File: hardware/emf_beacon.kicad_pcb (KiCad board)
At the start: 2 copper layers, 100 x 100 mm, 133 parts, among them J1 USB_C_Receptacle_USB2.0_16P, J10 Conn_01x02, J11 Conn_01x02, J12 Conn_01x02, J13 Conn_01x02, J14 Conn_01x02, J2 B6B-PH-SM4-TB, J3 B6B-PH-SM4-TB, J4 Conn_01x02, J5 Conn_01x02, J6 Conn_01x02, J7 Conn_01x02, J8 Conn_01x02, J9 Conn_01x02, Q1 AO3400A, Q10 AO3400A, Q12 DMP3013SFV, Q2 AO3400A, Q3 AO3400A, Q4 AO3400A, Q5 AO3400A, Q6 AO3400A, Q7 AO3400A, Q8 AO3400A, Q9 AO3400A, SW1 SW_DIP_x10, SW2 TS-1088-AR02016, U1 ESP32-C3-WROOM-02, U2 MCP23017T-E/SS, U4 PCA9685PW,118, U5 TPS565208, U6 CA-IS3092W, U7 TPS82140SILR

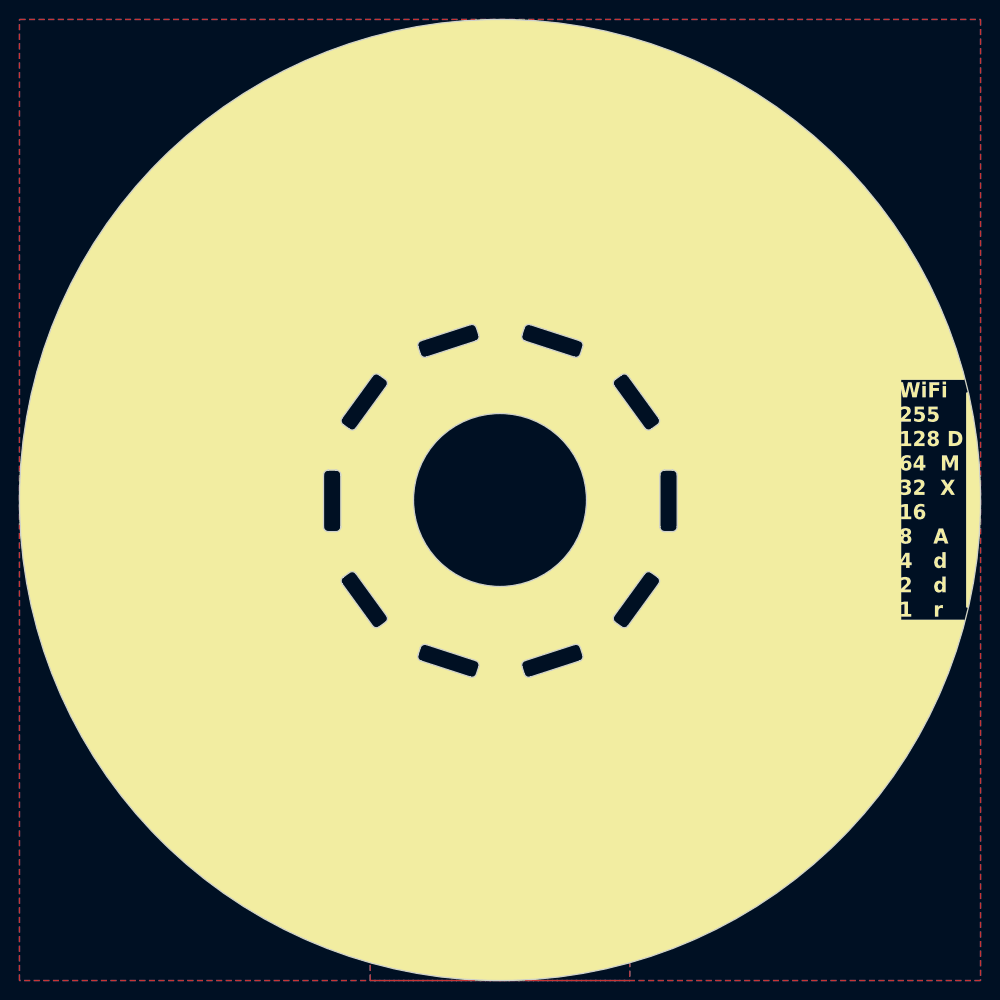
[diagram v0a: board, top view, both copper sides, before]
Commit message: finished USB routing
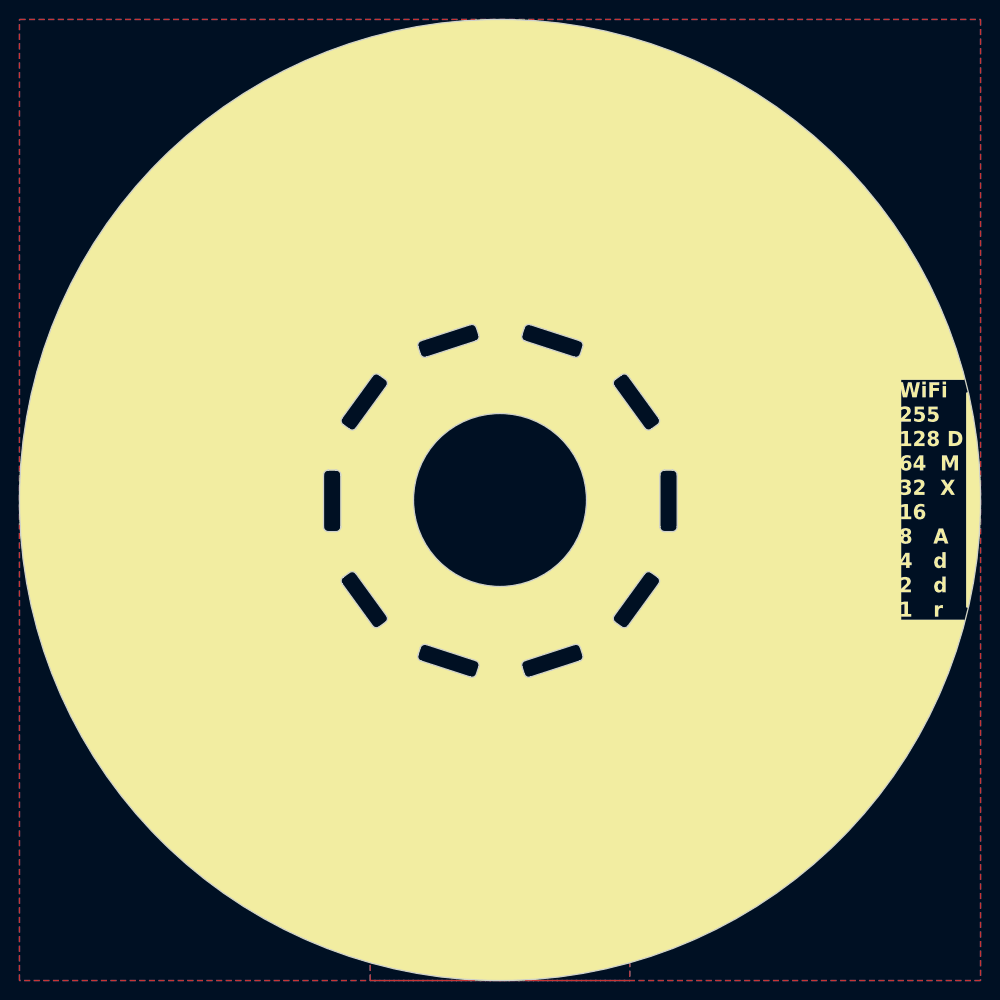
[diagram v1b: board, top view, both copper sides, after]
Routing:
- net /CTRL/USB-: track 19.7 -> 18.7 mm

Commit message: finished NTC routing
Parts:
- moved R3 2.02 mm to (134.8, 56.5), turned to -90 degrees
- moved C3 1.03 mm to (133.2, 56.5), turned to 90 degrees
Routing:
- net /CTRL/TEMP_MON: track 31.4 -> 60.6 mm, vias 1 -> 2
- net +3V3: track 236.9 -> 243.6 mm, vias 11 -> 12
- net GND: vias 117 -> 120
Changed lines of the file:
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@@
 	(footprint "Capacitor_SMD:C_0603_1608Metric"
 		(layer "B.Cu")
-		(at 134.25 56.25 -90)
+		(at 133.25 56.5 90)
 		(descr "Capacitor SMD 0603 (1608 Metric), square (rectangular) end terminal, IPC-7351 nominal, (Body size source: IPC-SM-782 page 76, https://www.pcb-3d.com/wordpress/wp-content/uploads/ipc-sm-782a_amendment_1_and_2.pdf), generated with kicad-footprint-generator")
 		(tags "capacitor")
 		(property "Reference" "C3"
-			(at 0 1.43 90)
+			(at 2.5 0 90)
 			(layer "B.SilkS")
 			(effects
@@
 		)
 		(property "MFR" ""
-			(at 0 0 270)
+			(at 0 0 90)
 			(unlocked yes)
 			(layer "B.Fab")
@@
 		)
 		(property "MPN" ""
-			(at 0 0 270)
+			(at 0 0 90)
 			(unlocked yes)
 			(layer "B.Fab")
@@
 		)
 		(property "LCSC" "C15849"
-			(at 0 0 270)
+			(at 0 0 90)
 			(unlocked yes)
 			(layer "B.Fab")
@@
 		(attr smd)
 		(fp_line
-			(start -0.14058 0.51)
-			(end 0.14058 0.51)
+			(start -0.14058 -0.51)
+			(end 0.14058 -0.51)
 			(stroke
 				(width 0.12)
@@
 		)
 		(fp_line
-			(start -0.14058 -0.51)
-			(end 0.14058 -0.51)
+			(start -0.14058 0.51)
+			(end 0.14058 0.51)
 			(stroke
 				(width 0.12)
@@
 		)
 		(pad "1" smd roundrect
-			(at -0.775 0 270)
+			(at -0.775 0 90)
 			(size 0.9 0.95)
 			(layers "B.Cu" "B.Mask" "B.Paste")
@@
 		)
 		(pad "2" smd roundrect
-			(at 0.775 0 270)
+			(at 0.775 0 90)
 			(size 0.9 0.95)
 			(layers "B.Cu" "B.Mask" "B.Paste")
@@
 	(footprint "Resistor_SMD:R_0603_1608Metric"
 		(layer "B.Cu")
-		(at 132.75 56.25 90)
+		(at 134.75 56.5 -90)
 		(descr "Resistor SMD 0603 (1608 Metric), square (rectangular) end terminal, IPC-7351 nominal, (Body size source: IPC-SM-782 page 72, https://www.pcb-3d.com/wordpress/wp-content/uploads/ipc-sm-782a_amendment_1_and_2.pdf), generated with kicad-footprint-generator")
 		(tags "resistor")
 		(property "Reference" "R3"
-			(at 0 1.43 90)
+			(at -2.5 0 90)
 			(layer "B.SilkS")
 			(effects
@@
 		)
 		(property "MFR" ""
-			(at 0 0 90)
+			(at 0 0 270)
 			(unlocked yes)
 			(layer "B.Fab")
@@
 		)
 		(property "MPN" ""
-			(at 0 0 90)
+			(at 0 0 270)
 			(unlocked yes)
 			(layer "B.Fab")
@@
 		)
 		(property "LCSC" "C25804"
-			(at 0 0 90)
+			(at 0 0 270)
 			(unlocked yes)
 			(layer "B.Fab")
@@
 		(attr smd)
 		(fp_line
-			(start -0.237258 -0.5225)
-			(end 0.237258 -0.5225)
+			(start -0.237258 0.5225)
+			(end 0.237258 0.5225)
 			(stroke
 				(width 0.12)
@@
 		)
 		(fp_line
-			(start -0.237258 0.5225)
-			(end 0.237258 0.5225)
+			(start -0.237258 -0.5225)
+			(end 0.237258 -0.5225)
 			(stroke
 				(width 0.12)
@@
 		)
 		(pad "1" smd roundrect
-			(at -0.825 0 90)
+			(at -0.825 0 270)
 			(size 0.8 0.95)
 			(layers "B.Cu" "B.Mask" "B.Paste")
@@
 		)
 		(pad "2" smd roundrect
-			(at 0.825 0 90)
+			(at 0.825 0 270)
 			(size 0.8 0.95)
 			(layers "B.Cu" "B.Mask" "B.Paste")
@@
 	)
 	(segment
-		(start 143.75 57.75)
-		(end 138.25 57.75)
-		(width 0.5)
-		(layer "F.Cu")
-		(net 1)
-	)
-	(segment
 		(start 177 122.25)
 		(end 180.75 122.25)
@@
 	)
 	(segment
+		(start 143.75 57.75)
+		(end 145.75 59.75)
+		(width 0.25)
+		(layer "F.Cu")
+		(net 1)
+	)
+	(segment
 		(start 164 61.5)
 		(end 164.75 62.25)
@@
 	)
 	(segment
-		(start 145.75 59.75)
-		(end 143.75 57.75)
-		(width 0.5)
+		(start 134.75 54.75)
+		(end 134.75 56.5)
+		(width 0.25)
 		(layer "F.Cu")
 		(net 1)
@@
 		(net 1)
 	)
+	(segment
+		(start 136 57.75)
+		(end 143.75 57.75)
+		(width 0.25)
+		(layer "F.Cu")
+		(net 1)
+	)
+	(segment
+		(start 134.75 56.5)
+		(end 136 57.75)
+		(width 0.25)
+		(layer "F.Cu")
+		(net 1)
+	)
 	(via
 		(at 123.75 78.75)
@@
 	)
 	(via
+		(at 134.75 54.75)
+		(size 0.6)
+		(drill 0.3)
+		(layers "F.Cu" "B.Cu")
+		(net 1)
+	)
+	(via
 		(at 165 56.5)
 		(size 0.6)
@@
 	)
 	(segment
+		(start 134.75 54.75)
+		(end 134.75 55.675)
+		(width 0.25)
+		(layer "B.Cu")
+		(net 1)
+	)
+	(segment
 		(start 187.975 76.75)
 		(end 187 76.75)
@@
 	)
 	(via
+		(at 124 60)
+		(size 0.6)
+		(drill 0.3)
+		(layers "F.Cu" "B.Cu")
+		(free yes)
+		(net 2)
+	)
+	(via
 		(at 146.25 125.25)
 		(size 0.6)
@@
 	)
 	(via
+		(at 133.25 54.75)
+		(size 0.6)
+		(drill 0.3)
+		(layers "F.Cu" "B.Cu")
+		(free yes)
+		(net 2)
+	)
+	(via
 		(at 111.25 109)
 		(size 0.6)
@@
 	)
 	(via
+		(at 144.25 59.5)
+		(size 0.6)
+		(drill 0.3)
+		(layers "F.Cu" "B.Cu")
+		(free yes)
+		(net 2)
+	)
+	(via
 		(at 161 59.75)
 		(size 0.6)
@@
 	)
 	(segment
-		(start 120.75 75.75)
-		(end 122 74.5)
+		(start 115.25 75.75)
+		(end 121.5 75.75)
 		(width 0.25)
 		(layer "F.Cu")
@@
 	)
 	(segment
-		(start 112.25 78.75)
-		(end 115.25 75.75)
+		(start 123.25 74)
+		(end 123.25 71.25)
 		(width 0.25)
 		(layer "F.Cu")
@@
 	)
 	(segment
-		(start 115.25 75.75)
-		(end 120.75 75.75)
+		(start 121.5 75.75)
+		(end 123.25 74)
+		(width 0.25)
+		(layer "F.Cu")
+		(net 84)
+	)
+	(segment
+		(start 112.25 78.75)
+		(end 115.25 75.75)
 		(width 0.25)
 		(layer "F.Cu")
@@
 	)
 	(via
+		(at 123.25 71.25)
+		(size 0.6)
+		(drill 0.3)
+		(layers "F.Cu" "B.Cu")
+		(net 84)
+	)
+	(via
 		(at 112.25 84.25)
 		(size 0.6)
@@
 	)
 	(segment
-		(start 141.25 57)
-		(end 137.5 57)
+		(start 133.3 57.325)
+		(end 134.75 57.325)
+		(width 0.25)
+		(layer "B.Cu")
+		(net 84)
+	)
+	(segment
+		(start 123.25 71.25)
+		(end 123.25 66.25)
+		(width 0.25)
+		(layer "B.Cu")
+		(net 84)
+	)
+	(segment
+		(start 133.25 57.275)
+		(end 133.3 57.325)
+		(width 0.25)
+		(layer "B.Cu")
+		(net 84)
+	)
+	(segment
+		(start 136.175 57.325)
+		(end 134.75 57.325)
+		(width 0.25)
+		(layer "B.Cu")
+		(net 84)
+	)
+	(segment
+		(start 123.25 66.25)
+		(end 122.75 65.75)
+		(width 0.25)
+		(layer "B.Cu")
+		(net 84)
+	)
+	(segment
+		(start 122.75 62.75)
+		(end 132.25 57.275)
 		(width 0.25)
 		(layer "B.Cu")
@@
 		(width 0.25)
 		(layer "B.Cu")
+		(net 84)
+	)
+	(segment
+		(start 122.75 65.75)
+		(end 122.75 62.75)
+		(width 0.25)
+		(layer "B.Cu")
+		(net 84)
+	)
+	(segment
+		(start 136.5 57)
+		(end 136.175 57.325)
+		(width 0.25)
+		(layer "B.Cu")
+		(net 84)
+	)
+	(segment
+		(start 141.25 57)
+		(end 136.5 57)
+		(width 0.25)
+		(layer "B.Cu")
+		(net 84)
+	)
+	(segment
+		(start 132.25 57.275)
+		(end 133.25 57.275)
+		(width 0.25)
+		(layer "B.Cu")

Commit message: ran DRC & DFM checks, looks good
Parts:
- moved D6 1.00 mm to (167.5, 64.5)
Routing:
- net Net-(D6-A): track 4.98 -> 5.98 mm
- net GND: vias 120 -> 122
- net +3V3: vias 12 -> 11
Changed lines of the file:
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@@
 			(unlocked yes)
 			(layer "B.SilkS")
+			(hide yes)
 			(effects
 				(font
@@
 			(unlocked yes)
 			(layer "B.SilkS")
+			(hide yes)
 			(effects
 				(font
@@
 		(tags "resistor")
 		(property "Reference" "TH1"
-			(at 0 1.43 90)
+			(at 0 -1.5 90)
 			(layer "B.SilkS")
 			(effects
@@
 	(footprint "Diode_SMD:D_SOD-323"
 		(layer "B.Cu")
-		(at 166.5 64.5 -90)
+		(at 167.5 64.5 -90)
 		(descr "SOD-323")
 		(tags "SOD-323")
@@
 		)
 		(fp_text user "${REFERENCE}"
-			(at 0 1.85 90)
+			(at 0 -1.75 90)
 			(layer "B.Fab")
 			(effects
@@
 			(unlocked yes)
 			(layer "B.SilkS")
+			(hide yes)
 			(effects
 				(font
@@
 			(unlocked yes)
 			(layer "B.SilkS")
+			(hide yes)
 			(effects
 				(font
@@
 		)
 		(fp_text user "${REFERENCE}"
-			(at 0 -2.5 180)
+			(at -1.25 -1.25 180)
 			(unlocked yes)
 			(layer "B.Fab")
@@
 			(unlocked yes)
 			(layer "B.SilkS")
+			(hide yes)
 			(effects
 				(font
@@
 			(unlocked yes)
 			(layer "B.SilkS")
+			(hide yes)
 			(effects
 				(font
@@
 			(unlocked yes)
 			(layer "B.SilkS")
+			(hide yes)
 			(effects
 				(font
@@
 			(unlocked yes)
 			(layer "B.SilkS")
+			(hide yes)
 			(effects
 				(font
@@
 			(unlocked yes)
 			(layer "B.SilkS")
+			(hide yes)
 			(effects
 				(font
@@
 			(unlocked yes)
 			(layer "B.SilkS")
+			(hide yes)
 			(effects
 				(font
@@
 	)
 	(via
-		(at 174.5 131.75)
-		(size 0.6)
-		(drill 0.3)
-		(layers "F.Cu" "B.Cu")
-		(net 1)
-	)
-	(via
 		(at 172.25 141)
 		(size 0.6)
@@
 	)
 	(via
+		(at 168.75 65.75)
+		(size 0.6)
+		(drill 0.3)
+		(layers "F.Cu" "B.Cu")
+		(free yes)
+		(net 2)
+	)
+	(via
 		(at 131.25 136)
 		(size 0.6)
@@
 	)
 	(via
+		(at 168.25 62.5)
+		(size 0.6)
+		(drill 0.3)
+		(layers "F.Cu" "B.Cu")
+		(free yes)
+		(net 2)
+	)
+	(via
 		(at 119 99.5)
 		(size 0.6)
@@
 	)
 	(segment
+		(start 166.5 61.5)
+		(end 167.5 62.5)
+		(width 0.25)
+		(layer "B.Cu")
+		(net 45)
+	)
+	(segment
 		(start 166.5 56.825)
 		(end 167.225 56.825)
@@
 	)
 	(segment
-		(start 167.725 57.325)
-		(end 167.725 59.5)
+		(start 167.5 62.5)
+		(end 167.5 63.45)
 		(width 0.25)
 		(layer "B.Cu")
@@
 	)
 	(segment
-		(start 165 59.075)
-		(end 165 60)
+		(start 167.725 57.325)
+		(end 167.725 59.5)
 		(width 0.25)
 		(layer "B.Cu")
@@
 	)
 	(segment
-		(start 166.5 61.5)
+		(start 165 59.075)
 		(end 165 60)
 		(width 0.25)
@@
 	)
 	(segment
-		(start 166.5 63.45)
-		(end 166.5 61.5)
+		(start 166.5 61.5)
+		(end 165 60)
 		(width 0.25)
 		(layer "B.Cu")
@@
 		(start 123.264898 119.689162)
 		(end 124.930635 121.3549)
-		(width 0.5)
+		(width 0.4)
 		(layer "B.Cu")
 		(net 59)
@@
 		(start 124.921663 121.085697)
 		(end 125.060751 121.224785)
-		(width 0.5)
+		(width 0.4)
 		(layer "B.Cu")
 		(net 59)
@@
 		(start 123.62868 122.37868)
 		(end 124.921663 121.085697)
-		(width 0.5)
+		(width 0.4)
 		(layer "B.Cu")
 		(net 59)
@@
 		(start 124.930635 121.3549)
 		(end 125.060751 121.224785)
-		(width 0.5)
+		(width 0.4)
 		(layer "B.Cu")
 		(net 59)
@@
 	)
 	(segment
-		(start 166.5 65.55)
-		(end 166.5 66.5)
+		(start 164.7 67.25)
+		(end 164.75 67.3)
 		(width 0.25)
 		(layer "B.Cu")
@@
 	)
 	(segment
-		(start 164.7 67.25)
-		(end 164.75 67.3)
+		(start 162.825 67.25)
+		(end 164.7 67.25)
 		(width 0.25)
 		(layer "B.Cu")
@@
 	)
 	(segment
-		(start 162.825 67.25)
-		(end 164.7 67.25)
+		(start 164.75 67.3)
+		(end 166.7 67.3)
 		(width 0.25)
 		(layer "B.Cu")
@@
 	)
 	(segment
-		(start 165.7 67.3)
-		(end 164.75 67.3)
+		(start 167.5 66.5)
+		(end 167.5 65.55)
 		(width 0.25)
 		(layer "B.Cu")
@@
 	)
 	(segment
-		(start 166.5 66.5)
-		(end 165.7 67.3)
+		(start 166.7 67.3)
+		(end 167.5 66.5)
 		(width 0.25)
 		(layer "B.Cu")

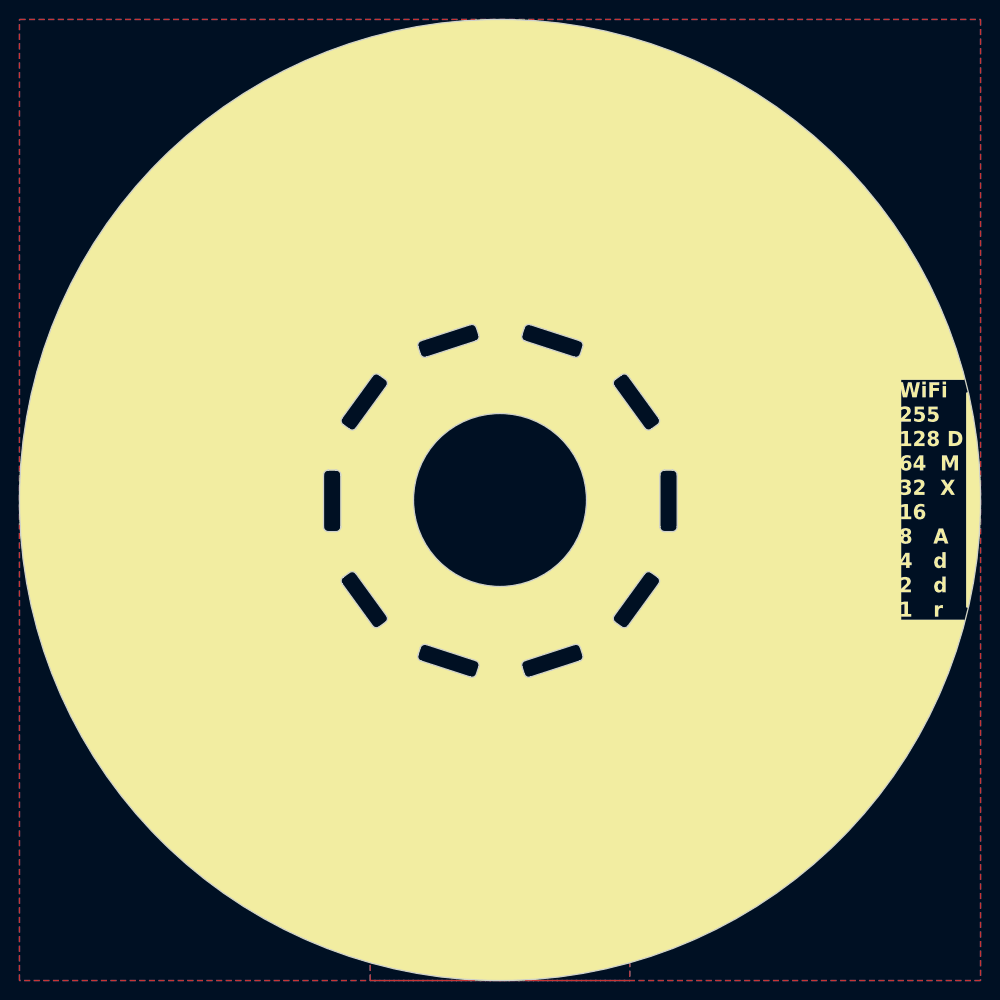
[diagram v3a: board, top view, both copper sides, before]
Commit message: adding stitching vias
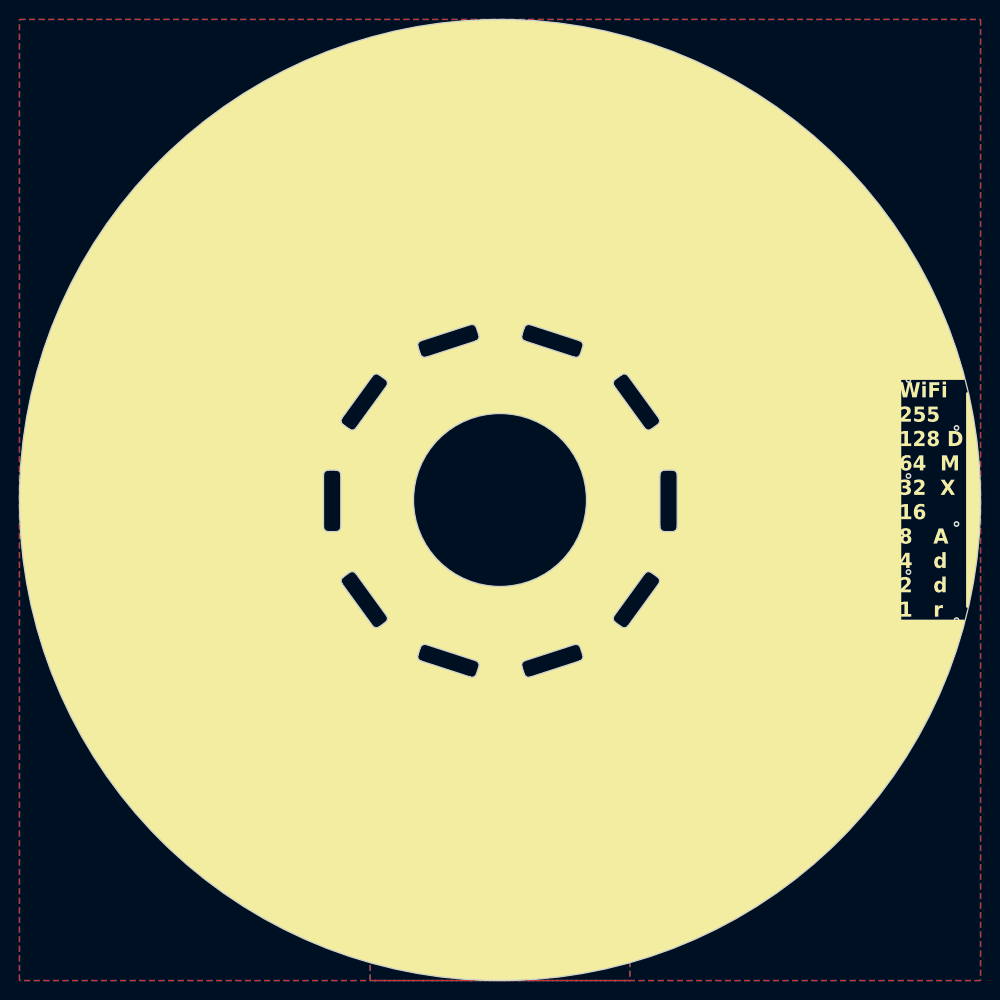
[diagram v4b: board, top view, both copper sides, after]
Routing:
- net GND: vias 122 -> 212
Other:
- board text added: "LED Beacon NullSector 2026 v0"
- board text removed: "LED Beacon Null Sector 2026 v0"

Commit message: unswapped LEDs
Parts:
- moved Q3 3.00 mm to (158.6, 121.6)
- moved Q8 3.00 mm to (141.4, 78.4)
- moved R19 3.00 mm to (146.8, 123.7)
- moved R24 3.00 mm to (153.2, 76.3)
- moved Q9 3.00 mm to (155.8, 77.4)
- moved R18 3.00 mm to (161.3, 121.0)
- moved R23 3.00 mm to (138.7, 79.0)
- moved Q10 3.00 mm to (167.9, 85.1)
- moved Q5 3.00 mm to (132.1, 114.9)
- moved Q7 3.00 mm to (130.3, 87.5)
- moved R20 3.00 mm to (133.5, 117.3)
- moved R25 3.00 mm to (166.5, 82.7)
- moved Q4 3.00 mm to (144.2, 122.6)
- moved Q1 3.00 mm to (173.2, 98.5)
- moved Q6 3.00 mm to (126.8, 101.5)
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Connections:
- J10 pad 1: +6V5 -> Net-(J10-Pin_1)
- J10 pad 2: Net-(J10-Pin_2) -> +6V5
- J11 pad 1: +6V5 -> Net-(J11-Pin_1)
- J11 pad 2: Net-(J11-Pin_2) -> +6V5
- J12 pad 1: +6V5 -> Net-(J12-Pin_1)
- J12 pad 2: Net-(J12-Pin_2) -> +6V5
- J13 pad 1: +6V5 -> Net-(J13-Pin_1)
- J13 pad 2: Net-(J13-Pin_2) -> +6V5
- J4 pad 1: +6V5 -> Net-(J4-Pin_1)
- J4 pad 2: Net-(J4-Pin_2) -> +6V5
- J5 pad 1: +6V5 -> Net-(J5-Pin_1)
- J5 pad 2: Net-(J5-Pin_2) -> +6V5
- J6 pad 1: +6V5 -> Net-(J6-Pin_1)
- J6 pad 2: Net-(J6-Pin_2) -> +6V5
- J7 pad 1: +6V5 -> Net-(J7-Pin_1)
- J7 pad 2: Net-(J7-Pin_2) -> +6V5
- J8 pad 1: +6V5 -> Net-(J8-Pin_1)
- J8 pad 2: Net-(J8-Pin_2) -> +6V5
- J9 pad 1: +6V5 -> Net-(J9-Pin_1)
- J9 pad 2: Net-(J9-Pin_2) -> +6V5
- Q1 pad 3: Net-(J4-Pin_2) -> Net-(J4-Pin_1)
- Q10 pad 3: Net-(J13-Pin_2) -> Net-(J13-Pin_1)
- Q2 pad 3: Net-(J5-Pin_2) -> Net-(J5-Pin_1)
- Q3 pad 3: Net-(J6-Pin_2) -> Net-(J6-Pin_1)
- Q4 pad 3: Net-(J7-Pin_2) -> Net-(J7-Pin_1)
- Q5 pad 3: Net-(J8-Pin_2) -> Net-(J8-Pin_1)
- Q6 pad 3: Net-(J9-Pin_2) -> Net-(J9-Pin_1)
- Q7 pad 3: Net-(J10-Pin_2) -> Net-(J10-Pin_1)
- Q8 pad 3: Net-(J11-Pin_2) -> Net-(J11-Pin_1)
- Q9 pad 3: Net-(J12-Pin_2) -> Net-(J12-Pin_1)
- R44 pad 1: Net-(J5-Pin_2) -> Net-(J5-Pin_1)
- R45 pad 1: Net-(J6-Pin_2) -> Net-(J6-Pin_1)
- R46 pad 1: Net-(J7-Pin_2) -> Net-(J7-Pin_1)
- R47 pad 1: Net-(J8-Pin_2) -> Net-(J8-Pin_1)
- R48 pad 1: Net-(J9-Pin_2) -> Net-(J9-Pin_1)
- R49 pad 1: Net-(J10-Pin_2) -> Net-(J10-Pin_1)
- R50 pad 1: Net-(J11-Pin_2) -> Net-(J11-Pin_1)
- R51 pad 1: Net-(J12-Pin_2) -> Net-(J12-Pin_1)
- R52 pad 1: Net-(J13-Pin_2) -> Net-(J13-Pin_1)
- R9 pad 1: Net-(J4-Pin_2) -> Net-(J4-Pin_1)
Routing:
- net Net-(J11-Pin_2): track 5.40 -> 0.00 mm
- net Net-(J6-Pin_2): track 5.40 -> 0.00 mm
- net Net-(J7-Pin_2): track 5.40 -> 0.00 mm
- net Net-(J12-Pin_2): track 5.40 -> 0.00 mm
- net Net-(J8-Pin_2): track 5.40 -> 0.00 mm
- net Net-(J13-Pin_2): track 5.40 -> 0.00 mm
- net Net-(J5-Pin_2): track 5.40 -> 0.00 mm
- net Net-(J10-Pin_2): track 5.40 -> 0.00 mm
- net Net-(J4-Pin_2): track 5.40 -> 0.00 mm
- net Net-(J9-Pin_2): track 5.40 -> 0.00 mm
- net Net-(J9-Pin_1): track 0.00 -> 5.01 mm
- net Net-(J4-Pin_1): track 0.00 -> 5.01 mm
- net Net-(J5-Pin_1): track 0.00 -> 5.01 mm
- net Net-(J10-Pin_1): track 0.00 -> 5.01 mm
- net Net-(J13-Pin_1): track 0.00 -> 5.01 mm
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
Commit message: preparing for release
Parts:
- added REF**: Untitled, emf_beacon_library:Untitled, B.Cu at (112.0, 125.5)
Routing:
- net GND: vias 213 -> 214
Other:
- board text added: "@pinski1_"
- board text added: "LED Beacon NullSector 2026 v1"
- board text removed: "LED Beacon NullSector 2026 v0"
